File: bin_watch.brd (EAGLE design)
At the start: 39.2 x 35.4 mm, 88 parts, among them IC1 MEGA48/88/168-AU, J1 USB3100-XX-X_REVB, Q1 32.768kHz, T1 2N7002BKV, T2 2N7002BKV, T3 2N7002BKV, T4 2N7002BKV, T5 PMDT670UPE, T6 PMDT670UPE, T7 PMDT670UPE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

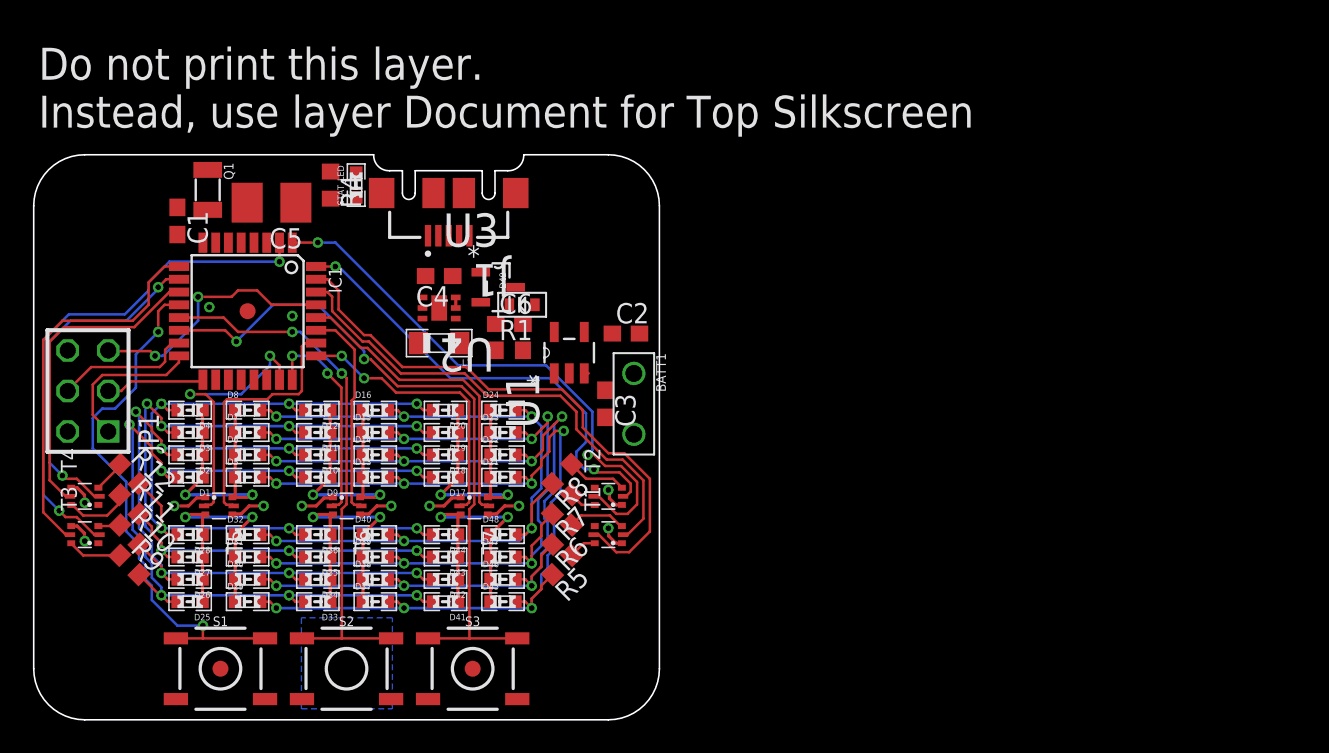
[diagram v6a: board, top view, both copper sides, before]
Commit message: QFN
ATmega328 now a QFN-32
TODO: place components, route
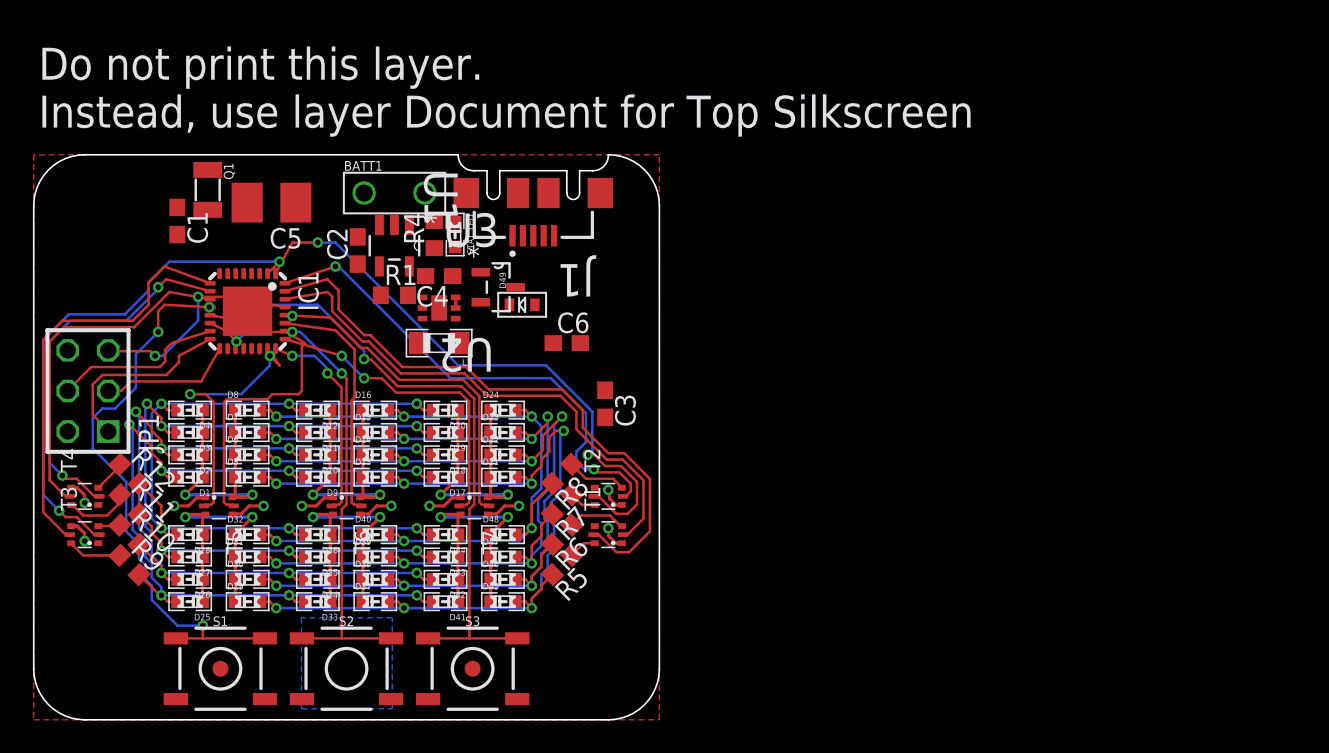
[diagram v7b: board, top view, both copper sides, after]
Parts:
- IC1: value MEGA48/88/168-AU -> MEGA48/88/168-MU; device avr-5:TQFP32-08 -> avr-5:MLF32
- moved BATT1 20.3 mm to (20.7, 33.0), turned to 0 degrees
- moved C2 17.6 mm to (20.3, 29.4), turned to 90 degrees
- moved U1 12.8 mm to (22.6, 29.7), turned to 270 degrees
- moved R1 7.98 mm to (22.6, 26.6)
- moved R4 7.20 mm to (25.1, 30.4), turned to 90 degrees
- moved STAT_LED 6.93 mm to (26.4, 30.4), turned to 270 degrees
- moved J1 5.30 mm to (31.3, 33.0)
- moved C6 3.79 mm to (33.4, 23.6)
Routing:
- net MISO: track 9.72 -> 11.9 mm
- net PD3: track 34.7 -> 36.9 mm
- net SCK: track 6.22 -> 8.43 mm
- net PD5: track 24.3 -> 26.4 mm
- net PD2: track 29.0 -> 31.2 mm
- net PC2: track 17.8 -> 19.9 mm
- net MOSI: track 8.67 -> 10.7 mm
- net PD1: track 35.3 -> 37.3 mm
- net PD6: track 21.4 -> 23.4 mm
- net PD7: track 19.8 -> 21.8 mm
- net PD0: track 30.7 -> 32.6 mm
- net PC4: track 13.2 -> 15.2 mm
- net PB0: track 33.5 -> 35.5 mm
- net PC5: track 19.6 -> 21.6 mm
- net RST: track 16.1 -> 14.2 mm
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- added copper zone on layer 1, net GND
- added copper zone on layer 15, net GND
- added copper zone on layer 2, net VCC
- removed copper zone on layer 2, net GND
- removed copper zone on layer 15, net VCC
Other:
- outline, holes or cut-outs redrawn

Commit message: Replaced AVR ISP with smaller pads
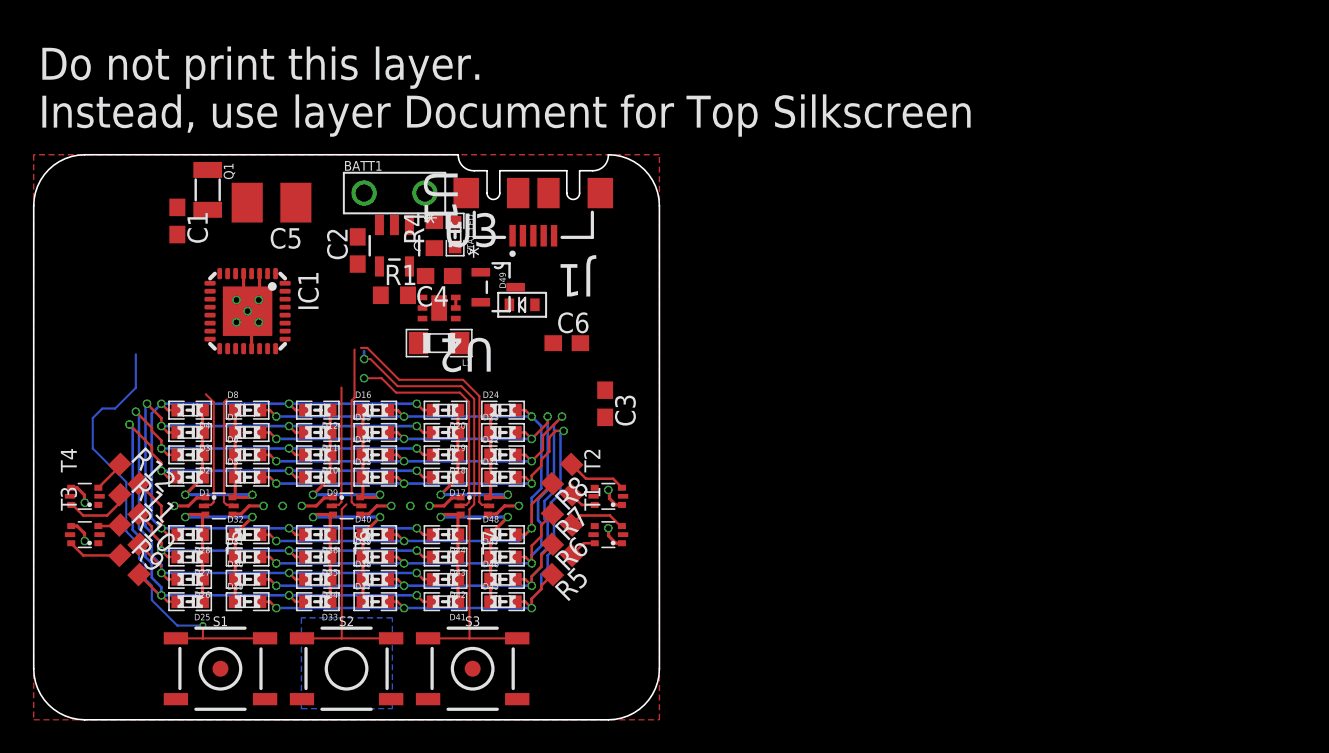
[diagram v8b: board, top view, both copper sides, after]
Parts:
- removed JP1: AVR-ISP-6, avr-5:AVR-ISP-6
- removed U$3: FIDUCIAL, adafruit:FIDUCIAL_1MM
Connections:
- net GND: no longer JP1.6
- net MISO: no longer JP1.1
- net MOSI: no longer JP1.4
- net RST: no longer JP1.5
- net SCK: no longer JP1.3
- net VCC: no longer JP1.2
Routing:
- net PD1: track 37.3 -> 0.00 mm
- net PD3: track 36.9 -> 0.00 mm, vias 2 -> 0
- net PD0: track 32.6 -> 0.00 mm
- net PD4: track 32.4 -> 0.00 mm, vias 2 -> 0
- net PD2: track 31.2 -> 0.00 mm, vias 2 -> 0
- net PD5: track 26.4 -> 0.00 mm
- net PD6: track 23.4 -> 0.00 mm, vias 2 -> 0
- net PD7: track 21.8 -> 0.00 mm
- net GND: track 6.04 -> 25.4 mm, vias 6 -> 11
- net PB1: track 32.2 -> 14.1 mm, vias 2 -> 0
- net RST: track 14.2 -> 0.00 mm, vias 2 -> 0
- net PB2: track 41.3 -> 29.2 mm, vias 2 -> 1
- net MISO: track 11.9 -> 0.00 mm
- net MOSI: track 10.7 -> 0.00 mm
- net PC0: track 17.1 -> 7.68 mm, vias 2 -> 0
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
